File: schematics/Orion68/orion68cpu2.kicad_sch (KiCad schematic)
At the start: 61 parts, among them J1 Euro96pin, J2 clock, J3 clock1, Q1 2N3904, Q2 2N3904, Q3 2N3904, SW2 sw_reset, U0 MC68000FN, U1 74LS245, U10 SST39SF010, U11 74HC74, U12 74LS393, U13 PAL20RS10, U2 74LS245, U3 74LS541, U4 74LS541, U5 74LS541, U6 74LS541, U7 74LS148, U8 GAL16V8, U9 SST39SF010

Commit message: Schematics update
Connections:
- net B/cpurw is gone; now on net B/cpuwr: J1.46
- net /cpu_bus_enable is gone; now on net /bus_enable: U3.19 (G2), U4.19 (G2), U5.19 (G2), U6.19 (G2)
- net B/AS: now also J1.43
- net B/LDS: now also J1.70
- net B/UDS: now also J1.71
- net GND: no longer U6.1 (G1)
- net /AS: now also U6.1 (G1); no longer J1.43
- net /LDS: no longer J1.70
- net /UDS: no longer J1.71
- net /bus_enable: now reaches U8.12 (IO8)
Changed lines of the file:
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@@
 		)
 	)
+	(polyline
+		(pts
+			(xy 360.045 14.605) (xy 360.045 72.39)
+		)
+		(stroke
+			(width 1)
+			(type dash)
+			(color 255 0 32 1)
+		)
+	)
 	(wire
 		(pts
@@
 	(wire
 		(pts
-			(xy 238.76 198.12) (xy 238.76 207.01)
-		)
-		(stroke
-			(width 0)
-			(type default)
-		)
-	)
-	(wire
-		(pts
 			(xy 49.53 265.43) (xy 49.53 275.59)
 		)
@@
 	(polyline
 		(pts
-			(xy 67.945 177.8) (xy 67.945 235.585)
+			(xy 71.12 177.8) (xy 71.12 235.585)
 		)
 		(stroke
@@
 		)
 	)
-	(label "{slash}LDS"
+	(label "B{slash}LDS"
 		(at 393.7 30.48 0)
 		(effects
@@
 		)
 	)
-	(label "{slash}cpu_bus_enable"
+	(label "{slash}bus_enable"
 		(at 278.13 54.61 180)
 		(effects
@@
 		)
 	)
+	(label "{slash}bus_enable"
+		(at 50.8 209.55 0)
+		(effects
+			(font
+				(size 1.27 1.27)
+				(thickness 0.254)
+				(bold yes)
+				(color 255 0 0 1)
+			)
+			(justify left bottom)
+		)
+	)
 	(label "IRQ6"
 		(at 396.24 81.28 0)
@@
 		)
 	)
+	(label "{slash}AS"
+		(at 238.76 198.12 180)
+		(effects
+			(font
+				(size 1.27 1.27)
+			)
+			(justify right bottom)
+		)
+	)
 	(label "AS"
 		(at 90.17 207.01 180)
@@
 		)
 	)
-	(label "{slash}cpu_bus_enable"
+	(label "{slash}bus_enable"
 		(at 236.22 200.66 180)
 		(effects
@@
 		)
 	)
-	(label "{slash}cpu_bus_enable"
+	(label "{slash}bus_enable"
 		(at 304.8 54.61 0)
 		(effects
@@
 		)
 	)
-	(label "{slash}cpu_bus_enable"
+	(label "{slash}bus_enable"
 		(at 236.22 54.61 180)
 		(effects
@@
 		)
 	)
-	(label "{slash}UDS"
+	(label "B{slash}UDS"
 		(at 393.7 33.02 0)
 		(effects
@@
 		)
 	)
-	(label "B{slash}cpurw"
+	(label "B{slash}cpuwr"
 		(at 383.54 50.8 0)
 		(effects
@@
 		)
 	)
-	(label "{slash}AS"
+	(label "B{slash}AS"
 		(at 383.54 43.18 0)
 		(effects
@@
 					(unit 1)
 				)
-			)
-		)
-	)
-	(symbol
-		(lib_id "power:GND")
-		(at 238.76 207.01 0)
-		(mirror y)
-		(unit 1)
-		(exclude_from_sim no)
-		(in_bom yes)
-		(on_board yes)
-		(dnp no)
-		(fields_autoplaced yes)
-		(property "Reference" "#PWR045"
-			(at 238.76 213.36 0)
-			(effects
-				(font
-					(size 1.27 1.27)
-				)
-				(hide yes)
-			)
-		)
-		(property "Value" "GND"
-			(at 238.76 212.09 0)
-			(effects
-				(font
-					(size 1.27 1.27)
-				)
-			)
-		)
-		(property "Footprint" ""
-			(at 238.76 207.01 0)
-			(effects
-				(font
-					(size 1.27 1.27)
-				)
-				(hide yes)
-			)
-		)
-		(property "Datasheet" ""
-			(at 238.76 207.01 0)
-			(effects
-				(font
-					(size 1.27 1.27)
-				)
-				(hide yes)
-			)
-		)
-		(property "Description" "Power symbol creates a global label with name \"GND\" , ground"
-			(at 238.76 207.01 0)
-			(effects
-				(font
-					(size 1.27 1.27)
-				)
-				(hide yes)
-			)
-		)
-		(pin "1"
-		)
-		(instances
-			(project "Orion68"
-				(path "/c7ab032b-c937-44de-ab42-c91dee57f0a8/d92fcd44-da66-430f-987f-be7edff43e49"
-					(reference "#PWR045")
-					(unit 1)
-				)

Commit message: Updating
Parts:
- J2: footprint (none) -> Connector_PinHeader_2.54mm:PinHeader_2x05_P2.54mm_Vertical
- J3: footprint (none) -> Connector_PinHeader_2.54mm:PinHeader_2x04_P2.54mm_Vertical
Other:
- note added: "CPU board - 0"
- note removed: "CPU board"
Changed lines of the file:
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@@
 		)
 	)
-	(text "CPU board"
+	(text "CPU board  -  0"
 		(exclude_from_sim no)
-		(at 310.642 255.778 0)
+		(at 314.452 256.54 0)
 		(effects
 			(font
 				(size 2 2)
+				(thickness 0.4)
+				(bold yes)
 			)
 		)
@@
 			)
 		)
-		(property "Footprint" ""
+		(property "Footprint" "Connector_PinHeader_2.54mm:PinHeader_2x04_P2.54mm_Vertical"
 			(at 101.6 69.85 0)
 			(effects
@@
 			)
 		)
-		(property "Footprint" ""
+		(property "Footprint" "Connector_PinHeader_2.54mm:PinHeader_2x05_P2.54mm_Vertical"
 			(at 92.71 45.72 0)
 			(effects

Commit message: Update
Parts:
- removed U13: PAL20RS10, Package_DIP:DIP-24_W7.62mm, symbol Logic_Programmable:PAL20RS10
- added U09: GAL20V8, Package_DIP:DIP-24_W7.62mm_Socket, symbol plds:GAL20V8
- renumbered U8 to U08
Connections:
- net +5V: now also U09.24 (VCC)
- net A0_148: now also U09.2 (I)
- net A1: now also U09.10 (I)
- net A1_148: now also U09.3 (I)
- net A2: now also U09.11 (I)
- net A2_148: now also U09.4 (I)
- net A3: now also U09.13 (I/~{OE})
- net AS: now also U09.9 (I)
- net D1: now also U08.12 (IO8)
- net GND: now also U09.12 (GND)
- net GS_148: now also U09.5 (I)
- net RESET: now also U09.18 (O); no longer U08.14 (IO6)
- net TICK_IN: now also U09.1 (I/CLK)
- net cpu_fc0: now also U09.6 (I)
- net cpu_fc1: now also U09.7 (I)
- net cpu_fc2: now also U09.8 (I)
- net /AS: no longer U1.19 (CE), U2.19 (CE)
- net /RESET: now also U09.14 (I); no longer U08.8 (I8)
- net /cpu_ipl0: now also U09.22 (O)
- net /cpu_ipl2: now also U09.20 (O)
- net /cpu_ipl1: now reaches U0.26 (~{IPL1})
- net /cpu_ipl1: now also U09.21 (O)
- net /ADDR_BUS_EN: now reaches U08.15 (IO5)
- net /ADDR_BUS_EN: now also U3.19 (G2), U4.19 (G2), U5.19 (G2), U6.19 (G2)
- removed net /bus_enable: U08.12 (IO8), U3.19 (G2), U4.19 (G2), U5.19 (G2), U6.19 (G2)
- new net /DATA_BUS_EN: U08.14 (IO6), U1.19 (CE), U2.19 (CE)
- no-connect marks 3 -> 8
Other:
- moved on the sheet: R3, U08

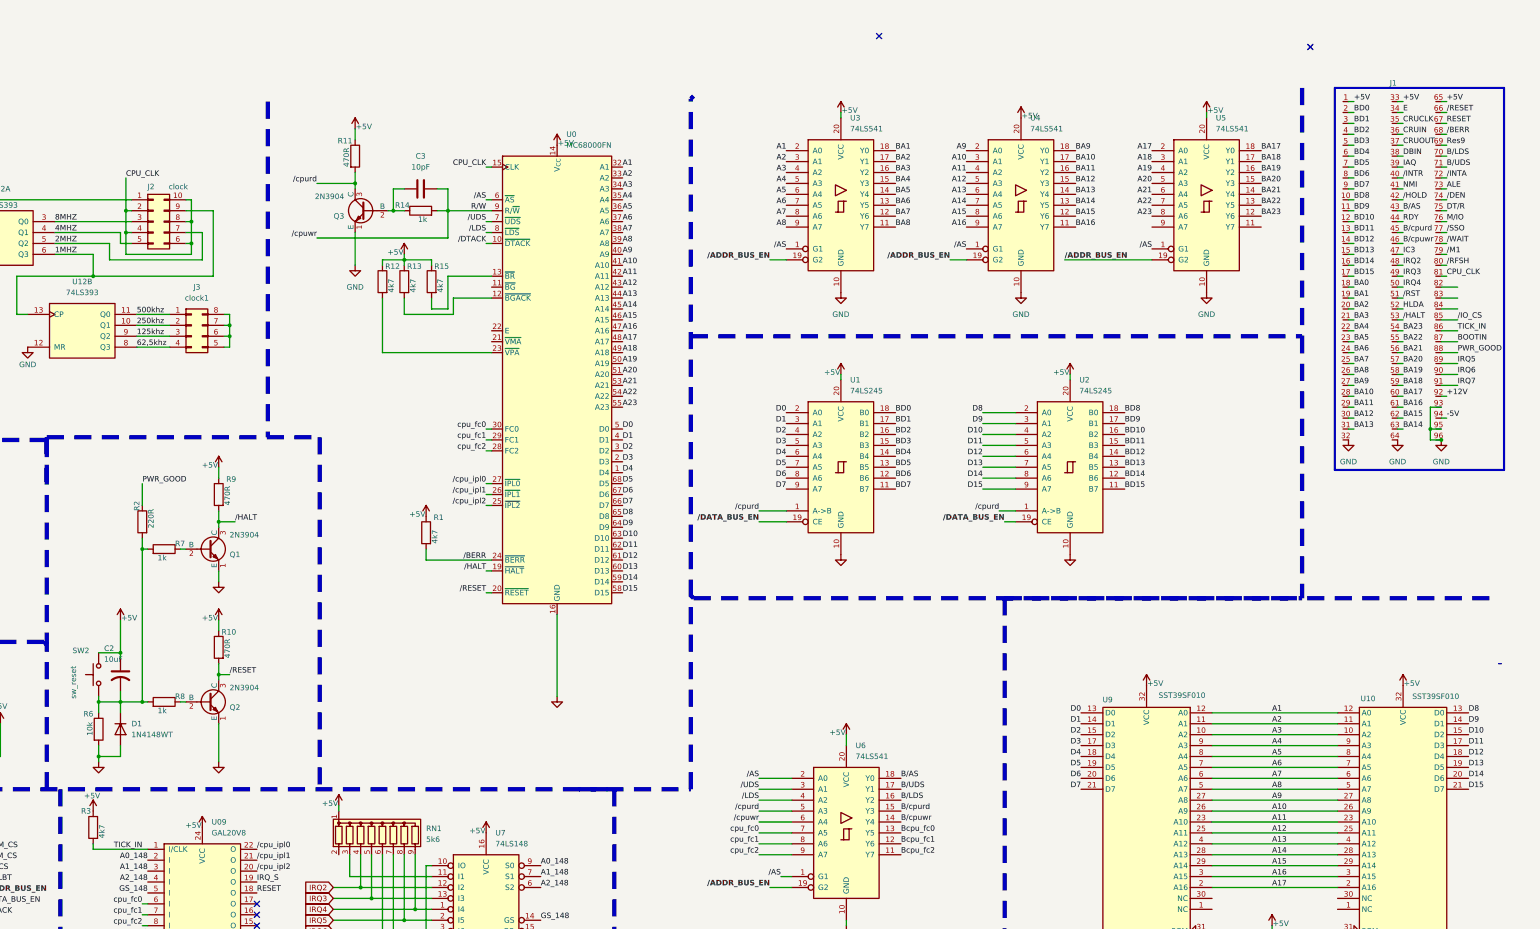
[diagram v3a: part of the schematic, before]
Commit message: Schematic verified to board
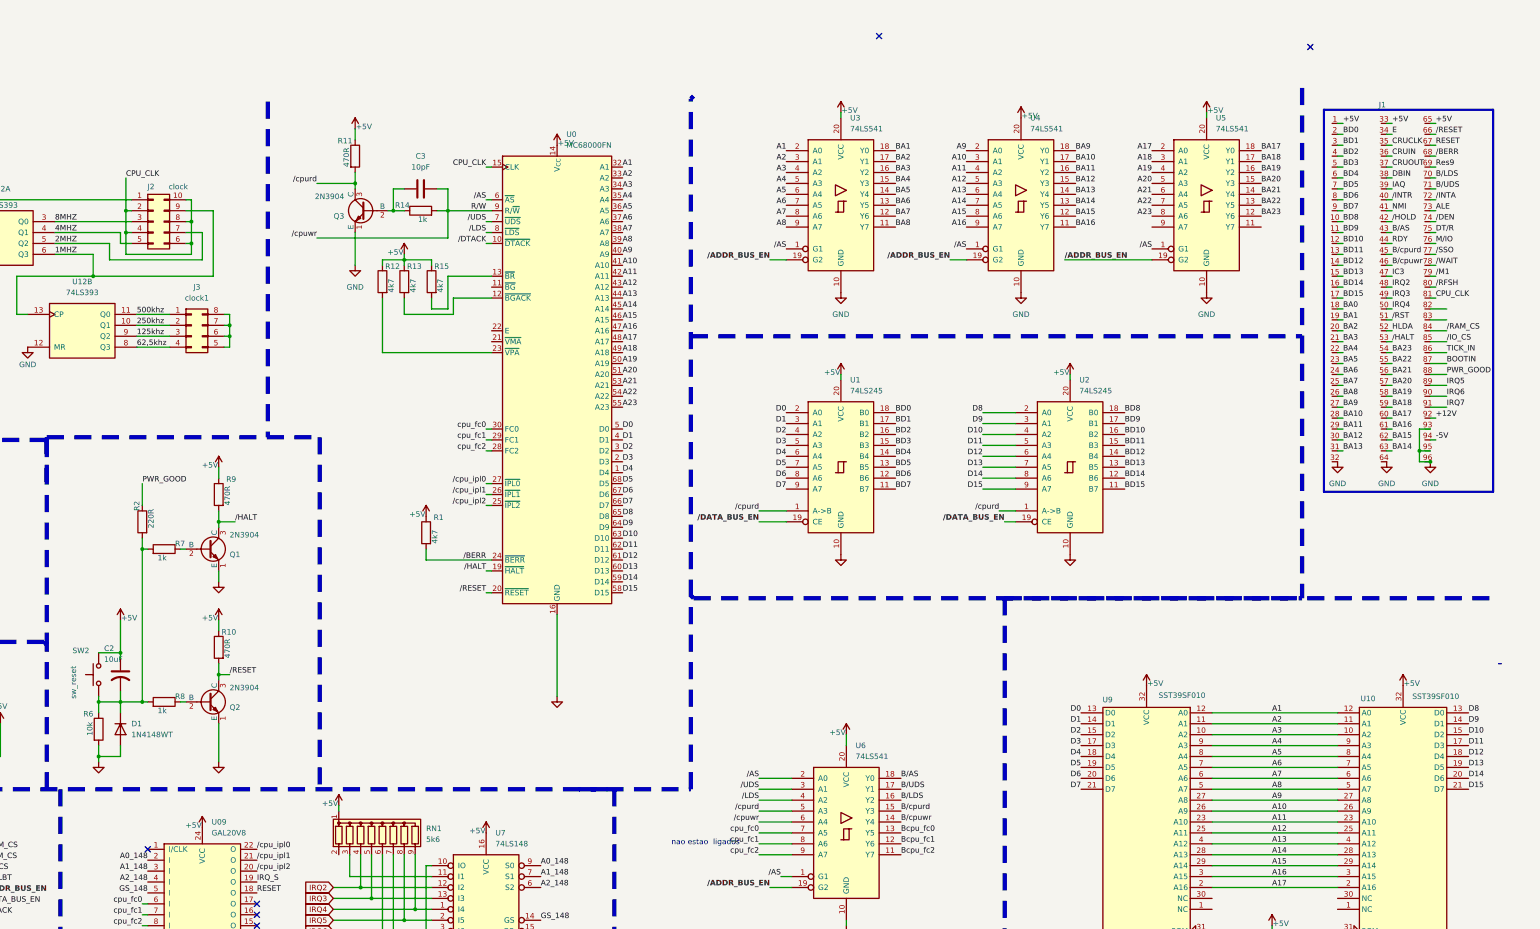
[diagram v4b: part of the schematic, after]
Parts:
- removed R3: 4k7, Resistor_THT:R_Axial_DIN0204_L3.6mm_D1.6mm_P5.08mm_Horizontal, symbol Device:R
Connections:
- net TICK_IN: no longer U09.1 (I/CLK)
- net /RAM_CS: now also J1.84
- no-connect marks 8 -> 9
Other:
- note added: "nao estao ligados"

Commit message: Cpu board fixed and running
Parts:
- added D5: Led_BusAddr, Diode_THT:D_T-1_P5.08mm_Horizontal, symbol Device:LED
- added R3: 270R, Resistor_THT:R_Axial_DIN0204_L3.6mm_D1.6mm_P5.08mm_Horizontal, symbol Device:R
- added U13, U14, U15: 74HC138, symbol 74xx:74HC138
- added U17: 74LS139, symbol 74xx:74LS139
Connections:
- net AS is gone; now on net /AS: U09.9 (I)
- net +5V: now also U11.10 (~{S}), U11.13 (~{R}), R3.2
- net 4MHZ: now also U11.11 (C); no longer U08.1 (I1/CLK)
- net D1: no longer U08.12 (IO8)
- net GND: now also U3.1 (G1), U4.1 (G1), U5.1 (G1), U5.9 (A7), U6.1 (G1)
- net R/W: now also U08.7 (I7)
- net /ADDR_BUS_EN: no longer U08.15 (IO5)
- net /AS: now also U11.12 (D); no longer U3.1 (G1), U4.1 (G1), U5.1 (G1), U6.1 (G1)
- net /DTACK: now also U11.9 (Q); no longer U08.13 (IO7)
- net /IO_CS: no longer J1.85
- net /KILLBT: now also U08.12 (IO8); no longer U08.16 (IO4)
- net /RAM_CS: no longer J1.84
- net /cpurd: now also U08.13 (IO7); no longer Q3.3 (C), R11.2
- net Addr_en: now reaches U5.11 (Y7)
- net Addr_en: now also D5.1 (K)
- new net: Q3.3 (C), R11.2
- new net: D5.2 (A), R3.1
- no-connect marks 9 -> 10
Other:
- note added: "VM"

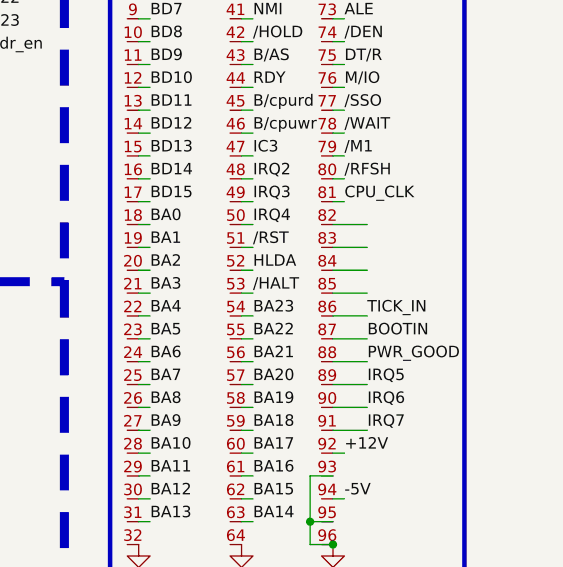
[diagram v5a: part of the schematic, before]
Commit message: A20 bug fixed, missing serial CSA, running ok
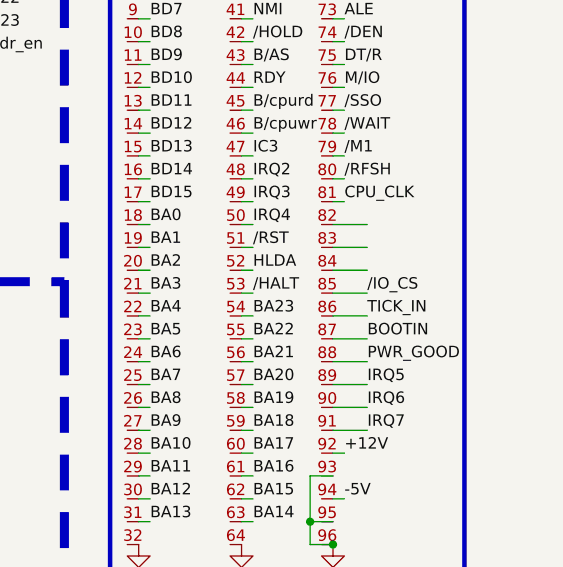
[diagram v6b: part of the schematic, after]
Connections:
- net /IO_CS: now also J1.85
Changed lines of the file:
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@@
+		)
+	)
+	(label "{slash}IO_CS"
+		(at 393.7 73.66 0)
+		(effects
+			(font
+				(size 1.27 1.27)
+			)
+			(justify left bottom)
 		)
 	)
